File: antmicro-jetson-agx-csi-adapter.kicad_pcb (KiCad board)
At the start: 4 copper layers, 105.1 x 105.5 mm, 98 parts, among them IC1 TCA9548ARGER, IC3 MAX1708EEE+, IC4 BNO055, IC5 RM24C128DS-LTAI-B, IC6 TCA9554ADBQR, IC7 Si7006-A20, J1 68715014522, J2 SM06B-SRSS-TB(LF)(SN), J3 68715014522, J4 SM09B-SRSS-TB(LF)(SN), J5 QTH-060-03-L-D-A, J6 *, J7 *, Q1 BSS138AKA

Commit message: Added PCB outline
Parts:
- removed C1, C2: CPol, C:_libraries_Libraries_pcblib_antmicro_capacitors_pol_Kemet_B.PcbLib_KEMET_B
- removed C12, C13, C14: 100n, C:_libraries_Libraries_pcblib_antmicro_capacitors_C.PcbLib_0603
- removed C15: 6n8, C:_libraries_antmicro-altium-components_Libraries_pcblib_antmicro_capacitors_C.PcbLib_0603
- removed C16, C6, C7, C8: 1u, C:_libraries_Libraries_pcblib_antmicro_capacitors_C.PcbLib_1206
- removed C17: 120n, C:_libraries_Libraries_pcblib_antmicro_capacitors_C.PcbLib_0603
- removed C18: 100n, Z:_home_piotr_ant_antmicro-altium-components_Libraries_pcblib_antmicro_capacitors_C.PcbLib_0603
- removed C19, C3, C4, C9: 100n, C:_libraries_Libraries_pcblib_antmicro_capacitors_C.PcbLib_0402
- removed C5: 220n, C:_libraries_Libraries_pcblib_antmicro_capacitors_C.PcbLib_0603
- removed D1: B340A-13-F, C:_libraries_libraries_pcblib_antmicro_passives_DO-214AC.PcbLib_DO-214AC
- removed IC1: TCA9548ARGER, C:_libraries_libraries_pcblib_antmicro_ic_VQFN-24.PcbLib_VQFN-24
- removed IC3: MAX1708EEE+, C:_libraries_Libraries_pcblib_antmicro_ic_MAX1708EEE.PcbLib_MAX1708EEE
- removed IC4: BNO055, C:_libraries_libraries_pcblib_antmicro_ic_BNO055.PcbLib_28LGA
- removed IC5: RM24C128DS-LTAI-B, C:_libraries_libraries_pcblib_antmicro_ic_TSSOP-8.PcbLib_TSSOP-8
- removed IC6: TCA9554ADBQR, AntmicroComponents.DbLib:DBQ0016A
- removed IC7: Si7006-A20, C:_libraries_libraries_pcblib_antmicro_ic_Si7006-A20.PcbLib_Si7006-A20
- removed J1, J3: 68715014522, C:_libraries_libraries_pcblib_antmicro_connectors_68715014522_FLIPPED.PcbLib_68715014522_FLIPPED
- removed J2: SM06B-SRSS-TB(LF)(SN), Z:_home_piotr_ant_antmicro-altium-components_libraries_pcblib_antmicro_connectors_SM06B-SRSS-TB.PcbLib_SM06B-SRSS-TB
- removed J4: SM09B-SRSS-TB(LF)(SN), AntmicroComponents.DbLib/antmicro_connectors:SM09B-SRSS-TB
- removed J5: QTH-060-03-L-D-A, AntmicroComponents.DbLib/antmicro_connectors:QTH-060-03-L-D-A
- removed J6: *, AntmicroComponents.DbLib/antmicro_pinheads:HEADER_1X6_male 2.54mm angle
- removed J7: *, Z:_home_piotr_ant_antmicro-altium-components_libraries_pcblib_antmicro_pinheads_HEADER_1X4_male 2.54mm angle.PcbLib_HEA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
- removed L1: IHLP2525CZER2R2M01, C:_libraries_libraries_pcblib_antmicro_passives_IHLP-2525CZ-01.PcbLib_IHLP-2525CZ-01
- removed Q1: BSS138AKA, Z:_home_piotr_ant_antmicro-altium-components_libraries_pcblib_antmicro_ic_SOT-23.PcbLib_SOT-23
- removed R1: 2R, C:_libraries_Libraries_pcblib_antmicro_resistors_R.PcbLib_0402
- removed R10, R11: 0R, AntmicroComponents.DbLib/antmicro_resistors:0402
- removed R12: 0R, C:_libraries_Libraries_pcblib_antmicro_resistors_R.PcbLib_1206
- removed R13, R15, R17, R19, R21, R30, R57, R58, R59, R60, R61: 0R, C:_libraries_Libraries_pcblib_antmicro_resistors_R.PcbLib_0402
- removed R14, R16, R2, R22, R23, R3, R6, R7: 2k, AntmicroComponents.DbLib/antmicro_resistors:0402
- removed R18, R20, R5: 2k2, C:_libraries_Libraries_pcblib_antmicro_resistors_R.PcbLib_0603
- removed R24, R25: 2k, Z:_home_piotr_ant_antmicro-altium-components_Libraries_pcblib_antmicro_resistors_R.PcbLib_0603
- removed R27, R4: 0R, C:_libraries_Libraries_pcblib_antmicro_resistors_R.PcbLib_0603
- removed R28, R29: 10k, C:_libraries_Libraries_pcblib_antmicro_resistors_R.PcbLib_0402
- removed R31, R32: 0R, Z:_home_piotr_ant_antmicro-altium-components_Libraries_pcblib_antmicro_resistors_R.PcbLib_0402
- removed R62, R63: 0R, Z:_home_hubert_hdd_hubert_Repos_antmicro-altium-components_Libraries_pcblib_antmicro_resistors_R.PcbLib_0402
- removed R8, R9: 2k, C:_libraries_Libraries_pcblib_antmicro_resistors_R.PcbLib_0603
- removed SP1, SP2, SP5, SP6: 9774110360, C:_libraries_libraries_pcblib_antmicro_mechanical_WE_9774110360.PcbLib_WE_9774110360
- removed TP10, TP12, TP13, TP14, TP3, TP30, TP4, TP5, TP6, TP7, TP8, TP9: Testpad, C:_libraries_libraries_pcblib_antmicro_passives_Testpad.PcbLib_TP-R-2
- removed TP15, TP16, TP17, TP18, TP19, TP20, TP21, TP22, TP23, TP24, TP29: Testpad, Z:_home_piotr_ant_antmicro-altium-components_libraries_pcblib_antmicro_passives_Testpad.PcbLib_TP-R-2
- added REF**: SAMTEC_QTH-060-03-X-D-A, antmicro-footprints:SAMTEC_QTH-060-03-X-D-A, F.Cu at (150.0, 77.1)
- added REF**: mounting-hole-3.5mm-NPTH, antmicro-footprints:mounting-hole-3.5mm-NPTH, F.Cu at (183.5, 73.0)
- added REF**: mounting-hole-3.5mm-NPTH, antmicro-footprints:mounting-hole-3.5mm-NPTH, F.Cu at (150.0, 105.2)
- added REF**: WE_68715014022, antmicro-footprints:WE_68715014022, B.Cu at (149.1, 78.3)
- added REF**: WE_68715014022, antmicro-footprints:WE_68715014022, B.Cu at (182.0, 92.0)
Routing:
- net CAM3_SDA: track 158.5 -> 0.00 mm, vias 3 -> 0
- net GND: track 158.3 -> 0.00 mm, vias 101 -> 0
- net CAM3_SCL: track 156.3 -> 0.00 mm, vias 2 -> 0
- net 3V3: track 155.8 -> 0.00 mm, vias 36 -> 0
- net CAM2_SDA: track 117.5 -> 0.00 mm, vias 1 -> 0
- net CAM2_SCL: track 114.5 -> 0.00 mm, vias 1 -> 0
- net MISC_I2C_SCL: track 81.3 -> 0.00 mm, vias 2 -> 0
- net 1V8: track 80.8 -> 0.00 mm, vias 6 -> 0
- net MISC_I2C_SDA: track 78.8 -> 0.00 mm, vias 3 -> 0
- net I2C_GP3_CLK: track 78.2 -> 0.00 mm, vias 2 -> 0
- net I2C_GP3_DAT: track 76.7 -> 0.00 mm, vias 2 -> 0
- net VSYNC_CAM1_3V3: track 52.5 -> 0.00 mm, vias 1 -> 0
- net VSYNC_CAM0_3V3: track 50.4 -> 0.00 mm, vias 1 -> 0
- net CSI3_D0_P: track 47.8 -> 0.00 mm, vias 1 -> 0
- net CSI3_D0_N: track 47.6 -> 0.00 mm, vias 1 -> 0
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- removed copper zone on B.Cu, net 3V3
- removed copper zone on F.Cu, net 3V3
- removed copper zone on In2.Cu, net 3V3
- removed copper zone on B.Cu, net 5V0
- removed copper zone on F.Cu, net 5V0
- removed copper zone on In2.Cu, net 5V0
- removed copper zone on F.Cu, net GND
- removed copper zone on In1.Cu, net GND
- removed copper zone on B.Cu, net NetC2_1
- removed copper zone on F.Cu, net NetC2_1
- removed copper zone on F.Cu, net NetD1_A
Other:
- board size 105.1 x 105.5 mm -> 73.6 x 41.1 mm
- copper layers 4 -> 2
- board text added: "CONNECTORS"
- board text removed: "0.010mm"
- board text removed: "0.035mm"
- board text removed: "0.036mm"
- board text removed: "0.110mm"
- board text removed: "1"
- board text removed: "1.130mm"
- board text removed: "1.6mm/1oz"
- board text removed: "10"
- board text removed: "11"
- board text removed: "12"
- board text removed: "13"
- board text removed: "2"
- board text removed: "3"
- board text removed: "3.5"
- board text removed: "4"
- board text removed: "4.3"
- board text removed: "5"
- board text removed: "6"
- board text removed: "7"
- board text removed: "8"
- board text removed: "9"
- board text removed: "Alvium Camera"
- board text removed: "Board Layer Stack"
- board text removed: "Bottom Overlay"
- board text removed: "Bottom Paste"
- board text removed: "Bottom Solder"
- board text removed: "Component Side"
- board text removed: "Constant"
- board text removed: "Copper"
- board text removed: "Depth cam sync"
- board text removed: "Dielectric 1"
- board text removed: "Dielectric 3"
- board text removed: "Dielectric 6"
- board text removed: "GND"
- board text removed: "Ground Layer"
- board text removed: "Layer"
- board text removed: "Liquid Lens"
- board text removed: "Material"
- board text removed: "Name"
- board text removed: "Power Layer"
- board text removed: "Rev.1.0.0"
- board text removed: "Solder Resist"
- board text removed: "Solder Side"
- board text removed: "Thickness"
- board text removed: "Top Overlay"
- board text removed: "Top Paste"
- board text removed: "Top Solder"
- board text removed: "Vsync_Cam0"
- board text removed: "Vsync_Cam1"
- board text removed: "Vsync_Cam2"
- board text removed: "Vsync_Cam3"

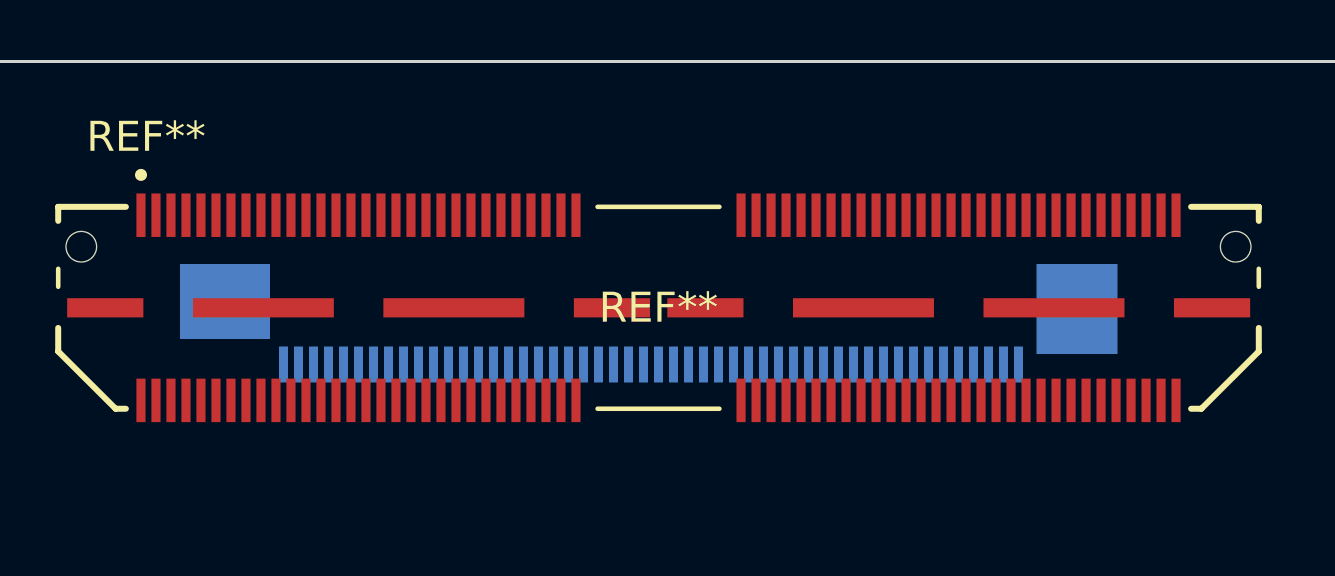
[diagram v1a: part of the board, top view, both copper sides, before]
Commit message: Added maximum height of components and fixed connector footprint on mockup pcb
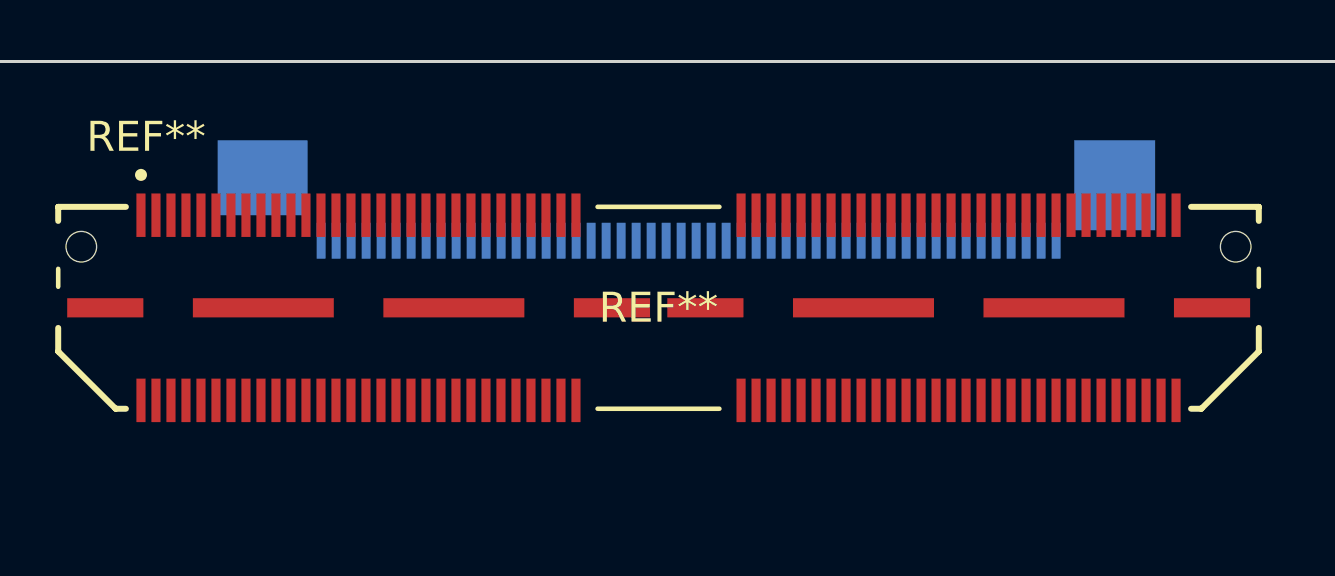
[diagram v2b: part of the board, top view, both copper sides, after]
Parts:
- removed the REF** at (149.1, 78.3)
- added REF**: WE_68715014522_ONE-SIDE, antmicro-footprints:WE_68715014522_ONE-SIDE, B.Cu at (151.0, 75.5)
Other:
- board text added: "Maximum bottom component height with QTH-060-03-H-A-D connector: 7.2mm Maximum top component height: 3mm but documentation is very vague and doesn't make sense; if taller components used reconsider this limit"

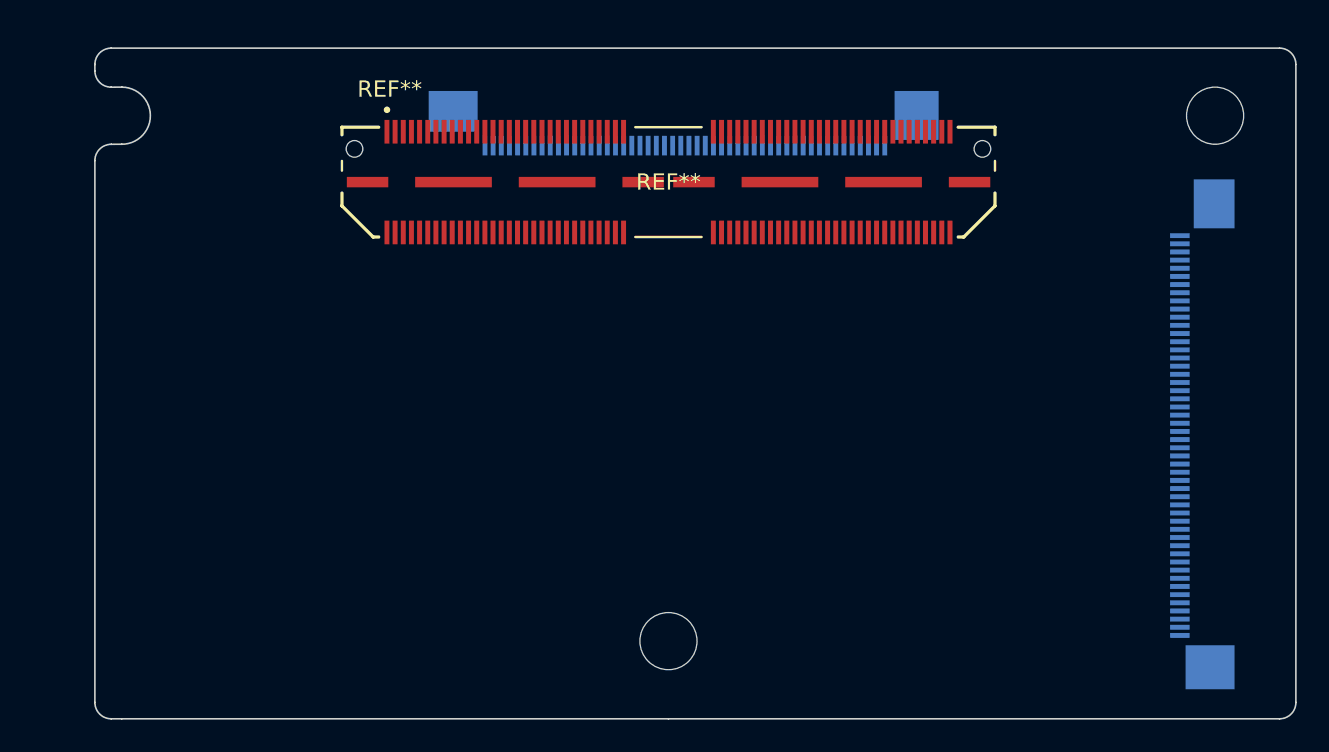
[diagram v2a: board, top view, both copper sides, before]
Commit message: Added logos and changed top and bottom side
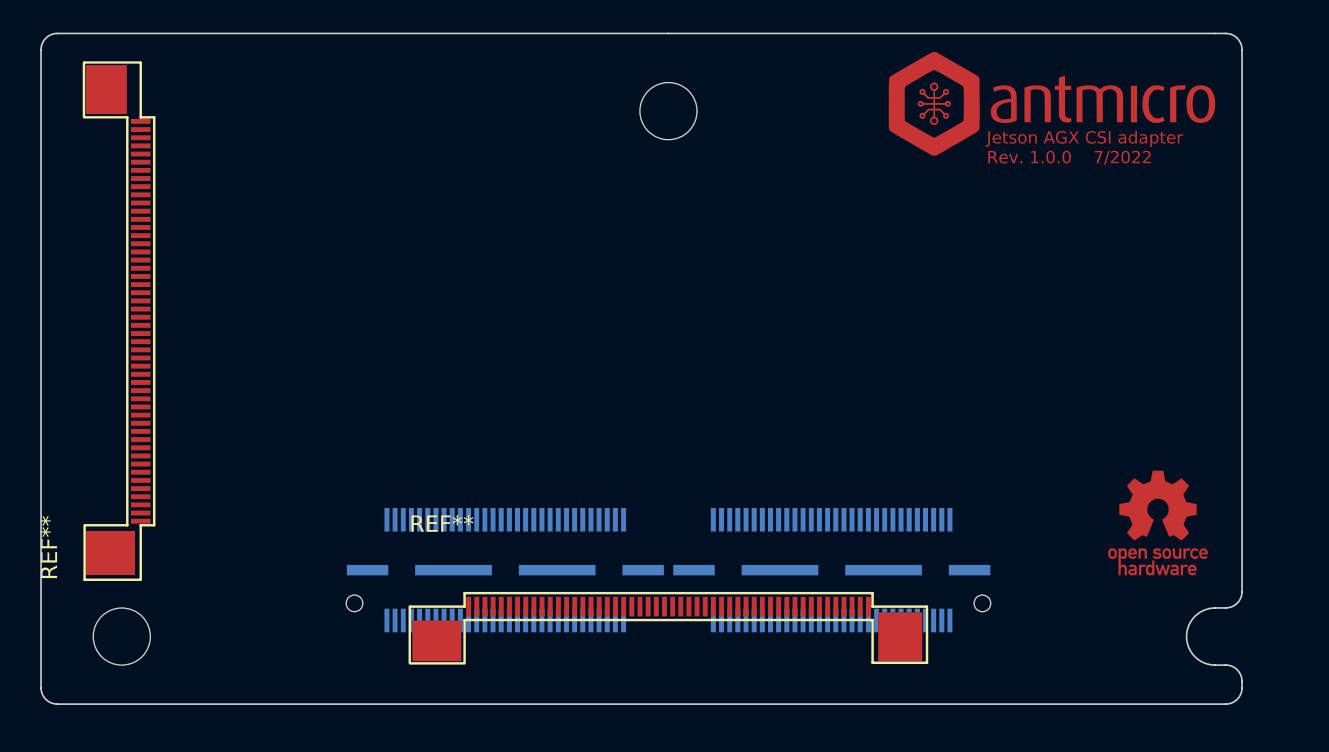
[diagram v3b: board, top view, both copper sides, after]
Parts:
- added G***: antmicro-logo_scaled_20mm, antmicro-footprints:antmicro-logo_scaled_20mm, F.Cu at (173.5, 72.5)
- added G***: LOGO, antmicro-footprints:oshw-logo, F.Cu at (180.0, 98.0)
- REF** (x2): moved to F.Cu
- REF**: moved to B.Cu
- moved REF** 74.2 mm to (116.5, 105.0), turned to 180 degrees
- moved REF** 65.4 mm to (117.0, 85.0)
- moved REF** 32.5 mm to (150.0, 72.8), turned to 180 degrees
- moved REF** 27.1 mm to (150.0, 102.5)
- moved REF** 23.8 mm to (150.0, 100.9)
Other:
- outline, holes or cut-outs redrawn
- board text added: "Jetson AGX CSI adapter Rev. 1.0.0 7/2022"

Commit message: Started PCB layout
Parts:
- removed the REF** at (150.0, 102.5)
- removed the REF** at (117.0, 85.0)
- removed the REF** at (150.0, 100.9)
- added C1: C_100n_0402, antmicro-footprints:0402-cap, F.Cu at (62.0, 92.0)
- added C10: C_220n_0402, antmicro-footprints:0402-cap, F.Cu at (72.5, 73.6)
- added C11: C_100n_0402, antmicro-footprints:0402-cap, F.Cu at (72.5, 77.6)
- added C12: 100n, antmicro-footprints:0603, F.Cu at (92.0, 68.5)
- added C13: C_220u_KEMET_D, antmicro-footprints:KEMET_D, F.Cu at (73.5, 64.7)
- added C14: 100n, antmicro-footprints:0603, F.Cu at (102.5, 62.8)
- added C15: C_10n_0402, antmicro-footprints:0402-cap, F.Cu at (98.9, 66.7)
- added C16: C_100n_0402, antmicro-footprints:0402-cap, F.Cu at (101.8, 66.7)
- added C17: C_100n_0402, antmicro-footprints:0402-cap, F.Cu at (105.2, 64.8)
- added C18: C_100n_0402, antmicro-footprints:0402-cap, F.Cu at (98.5, 68.7)
- added C19: 100n, antmicro-footprints:0402, F.Cu at (104.5, 66.6)
- added C2: C_100n_0402, antmicro-footprints:0402-cap, F.Cu at (63.2, 86.0)
- added C3: C_100n_0402, antmicro-footprints:0402-cap, F.Cu at (64.9, 94.0)
- added C4: C_1u_0603, antmicro-footprints:0603-cap, F.Cu at (66.3, 75.6)
- added C5: C_1u_0603, antmicro-footprints:0603-cap, F.Cu at (62.8, 78.0)
- added C6: C_1u_0603, antmicro-footprints:0603-cap, F.Cu at (62.8, 75.6)
- added C7: C_1u_0603, antmicro-footprints:0603-cap, F.Cu at (80.3, 67.2)
- added C8: C_220u_KEMET_D, antmicro-footprints:KEMET_D, F.Cu at (56.8, 68.8)
- added C9: C_100n_0402, antmicro-footprints:0402-cap, F.Cu at (72.5, 75.6)
- added D1: B340A-13-F, antmicro-footprints:DO-214AC, F.Cu at (82.6, 63.9)
- added IC1: MAX1708EEE+, antmicro-footprints:QSOP-16_3.9x4.9mm_P0.635mm, F.Cu at (66.0, 71.0)
- added J1: QTH-060-03-L-D-A, antmicro-footprints:SAMTEC_QTH-060-03-X-D-A, B.Cu at (150.0, 100.9)
- added J2: WE_68715014522_ONE-SIDE, antmicro-footprints:WE_68715014522_ONE-SIDE, F.Cu at (150.0, 102.5)
- added J3: SM06B-SRSS-TB(LF)(SN), antmicro-footprints:JST_SM06B-SRSS-TB(LF)(SN), F.Cu at (121.0, 78.0)
- added J4: WE_68715014022, antmicro-footprints:WE_68715014022, F.Cu at (183.0, 86.0)
- added J5: SM09B-SRSS-TB(LF)(SN), antmicro-footprints:JST_SM09B-SRSS-TB(LF)(SN), F.Cu at (116.9, 93.0)
- added J6: 61300611121, antmicro-footprints:61300611121, F.Cu at (166.3, 71.0)
- added L1: IHLP2525CZER2R2M01, antmicro-footprints:IHLP2525CZER, F.Cu at (56.1, 75.8)
- added Q1: BSS138AKA, antmicro-footprints:SOT-23-3, F.Cu at (72.6, 70.1)
- added R1: R_0R_0402, antmicro-footprints:0402-res, F.Cu at (60.2, 86.0)
- added R10: R_2k_0402, antmicro-footprints:0402-res, F.Cu at (59.1, 98.0)
- added R11: R_0R_0402, antmicro-footprints:0402-res, F.Cu at (67.8, 92.0)
- added R12: R_0R_0402, antmicro-footprints:0402-res, F.Cu at (71.9, 88.0)
- added R13: R_0R_0402, antmicro-footprints:0402-res, F.Cu at (58.6, 100.0)
- added R14: R_0R_0402, antmicro-footprints:0402-res, F.Cu at (59.1, 92.0)
- added R15: R_2k2_0402, antmicro-footprints:0402-res, F.Cu at (55.6, 99.9)
- added R16: R_2k2_0402, antmicro-footprints:0402-res, F.Cu at (57.3, 88.0)
- added R17: R_2k_0402, antmicro-footprints:0402-res, F.Cu at (59.1, 90.0)
- added R18: R_2k_0402, antmicro-footprints:0402-res, F.Cu at (62.0, 90.0)
- added R19: R_2k_0402, antmicro-footprints:0402-res, F.Cu at (62.0, 94.0)
- added R2: R_0R_0402, antmicro-footprints:0402-res, F.Cu at (69.0, 88.0)
- added R20: 2k2, antmicro-footprints:0603, F.Cu at (99.1, 62.8)
- added R21: R_2k_0402, antmicro-footprints:0402-res, F.Cu at (64.9, 90.0)
- added R22: R_0R_0402, antmicro-footprints:0402-res, F.Cu at (62.0, 96.0)
- added R23: R_0R_0402, antmicro-footprints:0402-res, F.Cu at (67.8, 90.0)
- added R24: R_0R_0402, antmicro-footprints:0402-res, F.Cu at (63.2, 88.0)
- added R25: R_0R_0402, antmicro-footprints:0402-res, F.Cu at (66.1, 86.0)
- added R26: R_2k_0402, antmicro-footprints:0402-res, F.Cu at (60.2, 88.0)
- added R27: 0R, antmicro-footprints:0603, F.Cu at (95.4, 68.5)
- added R28: R_2k_0402, antmicro-footprints:0402-res, F.Cu at (62.0, 98.0)
- added R29: R_2k_0402, antmicro-footprints:0402-res, F.Cu at (59.1, 96.0)
- added R3: R_0R_0402, antmicro-footprints:0402-res, F.Cu at (69.0, 86.0)
- added R30: R_2k_0402, antmicro-footprints:0402-res, F.Cu at (71.9, 86.0)
- added R31: R_2k_0402, antmicro-footprints:0402-res, F.Cu at (75.4, 73.6)
- added R32: R_2k_0402, antmicro-footprints:0402-res, F.Cu at (69.6, 77.6)
- added R33: R_0R_0402, antmicro-footprints:0402-res, F.Cu at (55.6, 80.8)
- added R34: R_0R_0402, antmicro-footprints:0402-res, F.Cu at (69.6, 75.3)
- added R35: R_0R_0402, antmicro-footprints:0402-res, F.Cu at (66.0, 77.8)
- added R36: R_0R_0402, antmicro-footprints:0402-res, F.Cu at (58.6, 80.8)
- added R37: R_2k_0402, antmicro-footprints:0402-res, F.Cu at (52.7, 80.8)
- added R38: R_2R_0402, antmicro-footprints:0402-res, F.Cu at (76.4, 68.6)
- added R39: R_2k_0402, antmicro-footprints:0402-res, F.Cu at (68.9, 79.6)
- added R4: 0R, antmicro-footprints:0603, F.Cu at (99.1, 64.7)
- added R40: R_0R_0402, antmicro-footprints:0402-res, F.Cu at (62.5, 80.3)
- added R41: R_10k_0402, antmicro-footprints:0402-res, F.Cu at (102.3, 64.7)
- added R42: R_0R_0402, antmicro-footprints:0402-res, F.Cu at (105.7, 62.8)
- added R43: R_10k_0402, antmicro-footprints:0402-res, F.Cu at (101.4, 68.7)
- added R5: R_0R_0402, antmicro-footprints:0402-res, F.Cu at (66.1, 88.0)
- added R6: R_0R_0402, antmicro-footprints:0402-res, F.Cu at (64.9, 92.0)
- added R7: R_0R_0402, antmicro-footprints:0402-res, F.Cu at (52.7, 99.9)
- added R8: R_10k_0402, antmicro-footprints:0402-res, F.Cu at (57.3, 86.0)
- added R9: R_2k_0402, antmicro-footprints:0402-res, F.Cu at (59.1, 94.0)
- added TP1: TP, antmicro-footprints:TP-R-1.5, F.Cu at (77.1, 88.8)
- added TP10: TP, antmicro-footprints:TP-R-1.5, F.Cu at (79.6, 88.8)
- added TP11: TP, antmicro-footprints:TP-R-1.5, F.Cu at (79.6, 86.3)
- added TP12: TP, antmicro-footprints:TP-R-1.5, F.Cu at (70.5, 90.3)
- added TP13: TP, antmicro-footprints:TP-R-1.5, F.Cu at (67.2, 99.2)
- added TP14: TP, antmicro-footprints:TP-R-1.5, F.Cu at (63.8, 101.2)
- added TP15: TP, antmicro-footprints:TP-R-1.5, F.Cu at (64.7, 98.7)
- added TP16: TP, antmicro-footprints:TP-R-1.5, F.Cu at (77.1, 86.3)
- added TP17: TP, antmicro-footprints:TP-R-1.5, F.Cu at (75.5, 91.3)
- added TP18: TP, antmicro-footprints:TP-R-1.5, F.Cu at (61.3, 100.2)
- added TP19: TP, antmicro-footprints:TP-R-1.5, F.Cu at (67.6, 94.2)
- added TP2: TP, antmicro-footprints:TP-R-1.5, F.Cu at (74.6, 88.8)
- added TP20: TP, antmicro-footprints:TP-R-1.5, F.Cu at (74.6, 86.3)
- added TP21: TP, antmicro-footprints:TP-R-1.5, F.Cu at (73.0, 91.3)
- added TP22: TP, antmicro-footprints:TP-R-1.5, F.Cu at (65.2, 80.5)
- added TP23: TP, antmicro-footprints:TP-R-1.5, F.Cu at (76.2, 70.9)
- added TP3: TP, antmicro-footprints:TP-R-1.5, F.Cu at (73.0, 93.8)
- added TP4: TP, antmicro-footprints:TP-R-1.5, F.Cu at (75.5, 93.8)
- added TP5: TP, antmicro-footprints:TP-R-1.5, F.Cu at (69.7, 97.8)
- added TP6: TP, antmicro-footprints:TP-R-1.5, F.Cu at (64.7, 96.2)
- added TP7: TP, antmicro-footprints:TP-R-1.5, F.Cu at (70.5, 92.8)
- added TP8: TP, antmicro-footprints:TP-R-1.5, F.Cu at (70.1, 95.3)
- added TP9: TP, antmicro-footprints:TP-R-1.5, F.Cu at (67.2, 96.7)
- added U1: NTS0102DP, antmicro-footprints:TSSOP-8_W3mm, F.Cu at (53.6, 88.8)
- added U2: PCA9547BS,118, antmicro-footprints:HVQFN24, F.Cu at (54.5, 95.7)
- added U3: BNO055, antmicro-footprints:LGA-28_5.2x3.8mm_BNO0055, F.Cu at (93.8, 64.7)
- moved REF** 67.0 mm to (183.5, 105.0)
- moved G*** 56.4 mm to (124.0, 104.5)
- moved G*** 38.5 mm to (135.0, 73.0)
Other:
- board size 73.6 x 41.1 mm -> 73.6 x 41 mm
- copper layers 2 -> 4
